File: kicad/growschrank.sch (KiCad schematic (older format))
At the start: 14 parts, among them J1 OLED, J2 BME280, J3 ESP8266, J4 DS3231, J5 Relais, J6 Rotary_Encoder, P1 Power, P2 Analog, P3 Digital, P4 Digital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

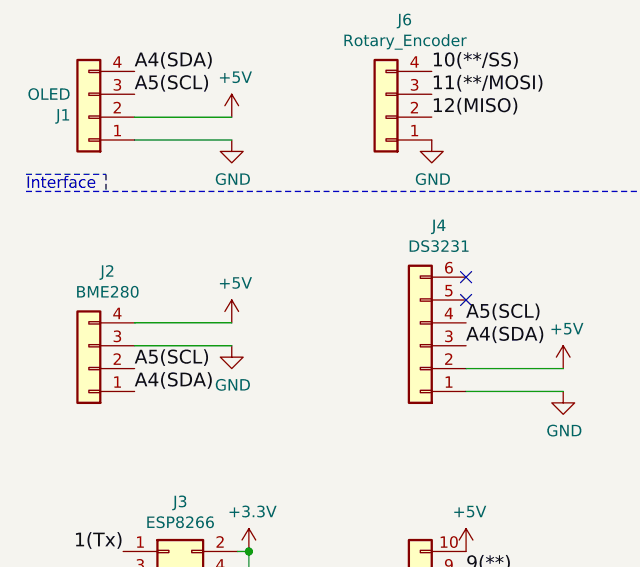
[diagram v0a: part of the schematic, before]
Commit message: Fixed power supply of BME280
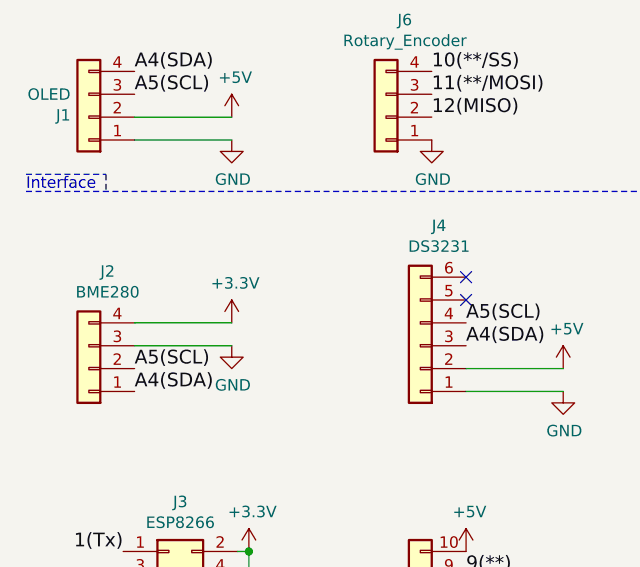
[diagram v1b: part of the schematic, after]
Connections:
- net +3V3: now also J2.4 (Pin_4)
- net +5V: no longer J2.4 (Pin_4)
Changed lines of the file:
@@
 	-1   0    0    1
-$EndComp
-$Comp
-L power:+5V #PWR08
-U 1 1 5F9B9C7E
-P 1375 1850
-F 0 "#PWR08" H 1375 1700 50  0001 C CNN
-F 1 "+5V" H 1390 2023 50  0000 C CNN
-F 2 "" H 1375 1850 50  0001 C CNN
-F 3 "" H 1375 1850 50  0001 C CNN
-	1    1375 1850
-	1    0    0    -1
 $EndComp
 Wire Wire Line
@@
 $EndComp
 Connection ~ 1450 2850
+$Comp
+L power:+3.3V #PWR?
+U 1 1 5FE0DEDF
+P 1375 1850
+F 0 "#PWR?" H 1375 1700 50  0001 C CNN
+F 1 "+3.3V" H 1390 2023 50  0000 C CNN
+F 2 "" H 1375 1850 50  0001 C CNN
+F 3 "" H 1375 1850 50  0001 C CNN
+	1    1375 1850
+	1    0    0    -1
+$EndComp
 $EndSCHEMATC

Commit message: GY-BME280 is 3.3V-5V fuck this shit
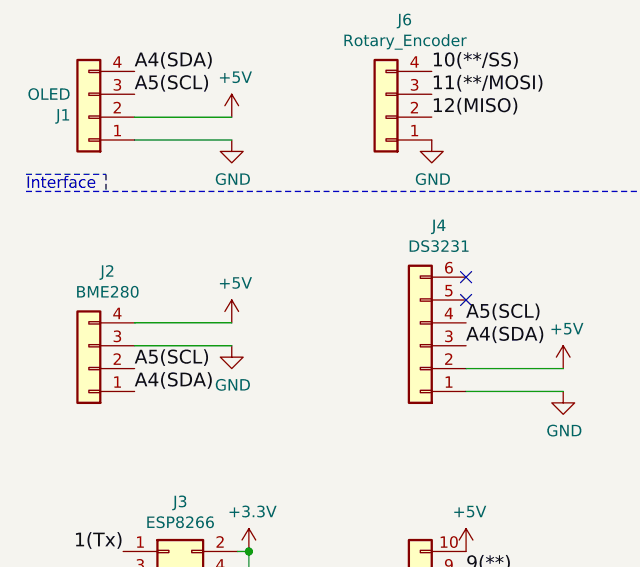
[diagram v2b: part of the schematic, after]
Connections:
- net +3V3: no longer J2.4 (Pin_4)
- net +5V: now also J2.4 (Pin_4)
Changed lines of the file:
@@
 Connection ~ 1450 2850
 $Comp
-L power:+3.3V #PWR?
-U 1 1 5FE0DEDF
+L power:+5V #PWR?
+U 1 1 5FE26E9C
 P 1375 1850
 F 0 "#PWR?" H 1375 1700 50  0001 C CNN
-F 1 "+3.3V" H 1390 2023 50  0000 C CNN
+F 1 "+5V" H 1390 2023 50  0000 C CNN
 F 2 "" H 1375 1850 50  0001 C CNN
 F 3 "" H 1375 1850 50  0001 C CNN

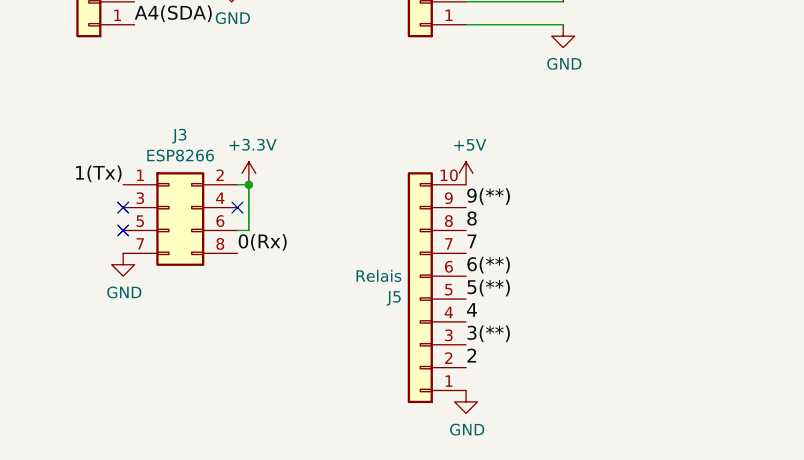
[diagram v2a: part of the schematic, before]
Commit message: Changed relais connector
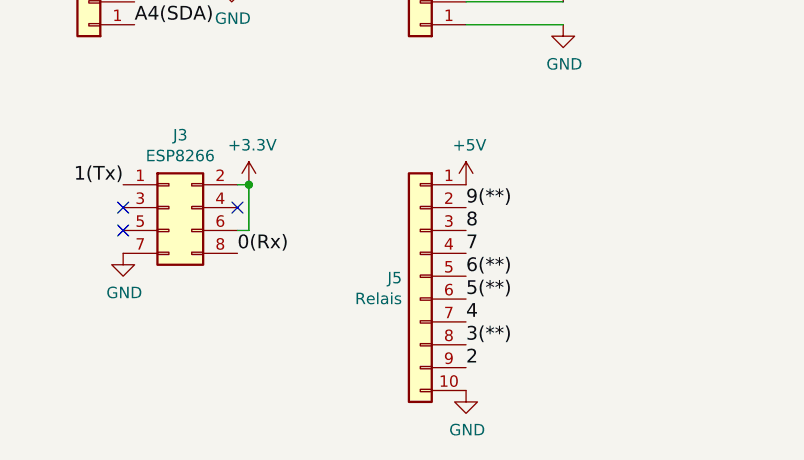
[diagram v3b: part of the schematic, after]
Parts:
- J1, J2, J6: footprint Connector_JST:JST_PH_B4B-PH-K_1x04_P2.00mm_Vertical -> Connector_JST:JST_XH_B4B-XH-A_1x04_P2.50mm_Vertical
- J5: footprint Connector_PinHeader_2.54mm:PinHeader_1x10_P2.54mm_Vertical -> Connector_JST:JST_XH_B10B-XH-A_1x10_P2.50mm_Vertical
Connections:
- net +5V: now also J5.1 (Pin_1); no longer J5.10 (Pin_10)
- net 2: now also J5.9 (Pin_9); no longer J5.2 (Pin_2)
- net 3(**): now also J5.8 (Pin_8); no longer J5.3 (Pin_3)
- net 4: now also J5.7 (Pin_7); no longer J5.4 (Pin_4)
- net 5(**): now also J5.6 (Pin_6); no longer J5.5 (Pin_5)
- net 6(**): now also J5.5 (Pin_5); no longer J5.6 (Pin_6)
- net 7: now also J5.4 (Pin_4); no longer J5.7 (Pin_7)
- net 8: now also J5.3 (Pin_3); no longer J5.8 (Pin_8)
- net 9(**): now also J5.2 (Pin_2); no longer J5.9 (Pin_9)
- net GND: now also J5.10 (Pin_10); no longer J5.1 (Pin_1)
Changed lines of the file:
@@
 F 0 "J1" H 830 942 50  0000 L CNN
 F 1 "OLED" H 830 851 50  0000 L CNN
-F 2 "Connector_JST:JST_PH_B4B-PH-K_1x04_P2.00mm_Vertical" H 750 950 50  0001 C CNN
+F 2 "Connector_JST:JST_XH_B4B-XH-A_1x04_P2.50mm_Vertical" H 750 950 50  0001 C CNN
 F 3 "~" H 750 950 50  0001 C CNN
 	1    750  950
@@
 L Connector_Generic:Conn_01x10 J5
 U 1 1 5F9B09E4
-P 2200 3350
-F 0 "J5" H 2280 3342 50  0000 L CNN
-F 1 "Relais" H 2280 3251 50  0000 L CNN
-F 2 "Connector_PinHeader_2.54mm:PinHeader_1x10_P2.54mm_Vertical" H 2200 3350 50  0001 C CNN
-F 3 "~" H 2200 3350 50  0001 C CNN
-	1    2200 3350
-	-1   0    0    1
+P 2200 3250
+F 0 "J5" H 2280 3242 50  0000 L CNN
+F 1 "Relais" H 2280 3151 50  0000 L CNN
+F 2 "Connector_JST:JST_XH_B10B-XH-A_1x10_P2.50mm_Vertical" H 2200 3250 50  0001 C CNN
+F 3 "~" H 2200 3250 50  0001 C CNN
+	1    2200 3250
+	-1   0    0    -1
 $EndComp
 $Comp
@@
 F 0 "J2" H 668 1625 50  0000 C CNN
 F 1 "BME280" H 668 1716 50  0000 C CNN
-F 2 "Connector_JST:JST_PH_B4B-PH-K_1x04_P2.00mm_Vertical" H 750 2050 50  0001 C CNN
+F 2 "Connector_JST:JST_XH_B4B-XH-A_1x04_P2.50mm_Vertical" H 750 2050 50  0001 C CNN
 F 3 "~" H 750 2050 50  0001 C CNN
 	1    750  2050
@@
 F 0 "J6" H 1968 525 50  0000 C CNN
 F 1 "Rotary_Encoder" H 1968 616 50  0000 C CNN
-F 2 "Connector_JST:JST_PH_B4B-PH-K_1x04_P2.00mm_Vertical" H 2050 950 50  0001 C CNN
+F 2 "Connector_JST:JST_XH_B4B-XH-A_1x04_P2.50mm_Vertical" H 2050 950 50  0001 C CNN
 F 3 "~" H 2050 950 50  0001 C CNN
 	1    2050 950
@@
 Connection ~ 1450 2850
 $Comp
-L power:+5V #PWR?
+L power:+5V #PWR0102
 U 1 1 5FE26E9C
 P 1375 1850
-F 0 "#PWR?" H 1375 1700 50  0001 C CNN
+F 0 "#PWR0102" H 1375 1700 50  0001 C CNN
 F 1 "+5V" H 1390 2023 50  0000 C CNN
 F 2 "" H 1375 1850 50  0001 C CNN
